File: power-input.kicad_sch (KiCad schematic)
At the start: 23 parts, among them J802 Conn_01x04, U202 XL1509-3.3

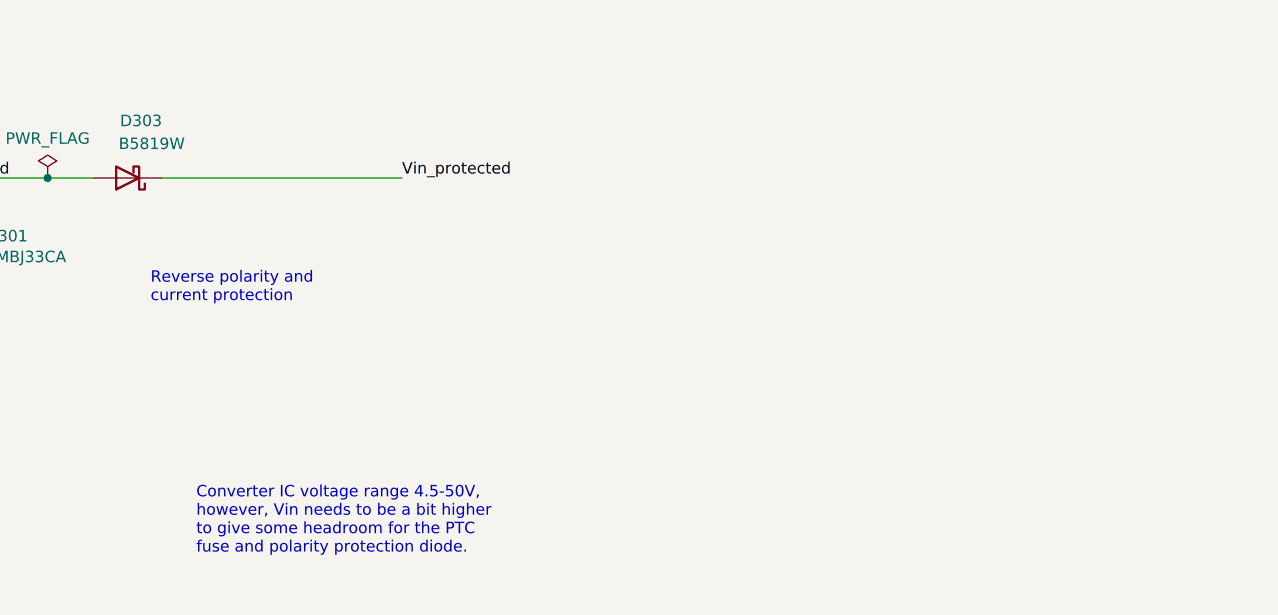
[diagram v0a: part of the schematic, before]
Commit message: Initial V1.0.0 Bluefin forked
Added ICM-42688-P 6-axis IMU
Added LM317 LDO for 6.4v or 5v MHU supply (selectable via jumper)
Added External LED's for IO2 (Pin 24) and 3.3v
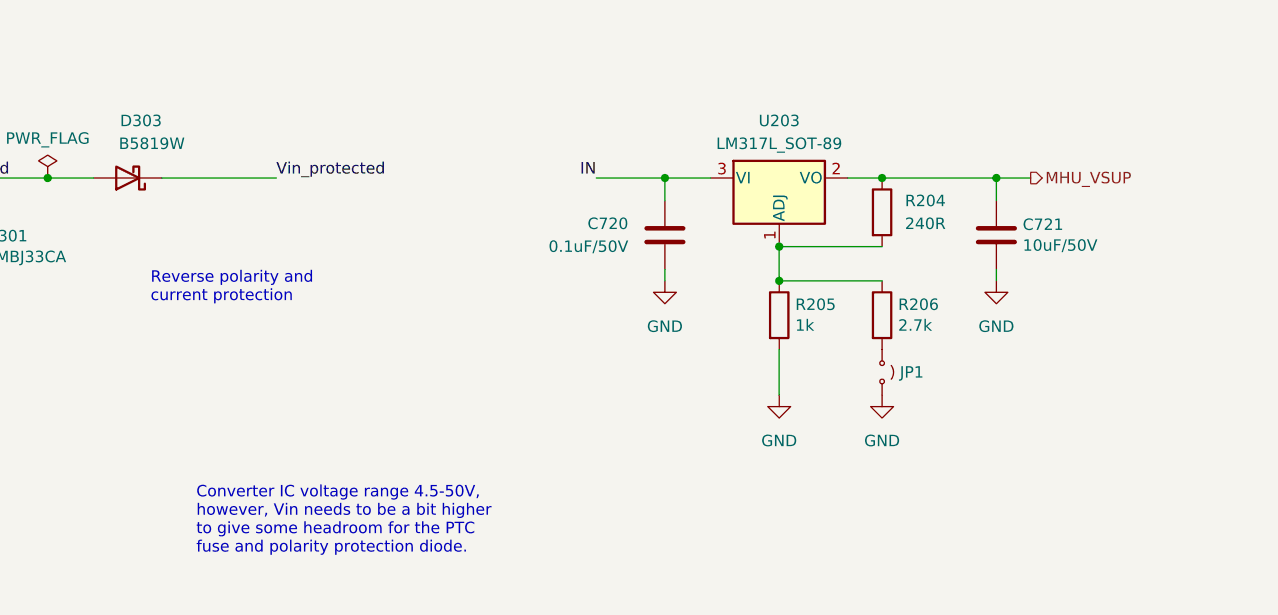
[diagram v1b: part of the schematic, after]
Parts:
- added C720: 0.1uF/50V, Capacitor_SMD:C_1206_3216Metric, symbol Device:C
- added C721: 10uF/50V, Capacitor_SMD:C_1206_3216Metric, symbol Device:C
- added JP1: Jumper_2_Small_Open, Connector_PinHeader_1.00mm:PinHeader_1x02_P1.00mm_Vertical, symbol Jumper:Jumper_2_Small_Open
- added R204: 240R, Resistor_SMD:R_0402_1005Metric, symbol Device:R
- added R205: 1k, Resistor_SMD:R_0402_1005Metric, symbol Device:R
- added R206: 2.7k, Resistor_SMD:R_0402_1005Metric, symbol Device:R
- added U203: LM317L_SOT-89, Package_TO_SOT_SMD:SOT-89-3, symbol Regulator_Linear:LM317L_SOT-89
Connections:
- net GND: now also C720.2, C721.2, JP1.2 (B), R205.2
- net IN: now also C720.1, U203.3 (VI)
- new net: JP1.1 (A), R206.2
- new net: R204.2, R205.1, R206.1, U203.1 (ADJ)
- new net MHU_VSUP: C721.1, R204.1, U203.2 (VO)

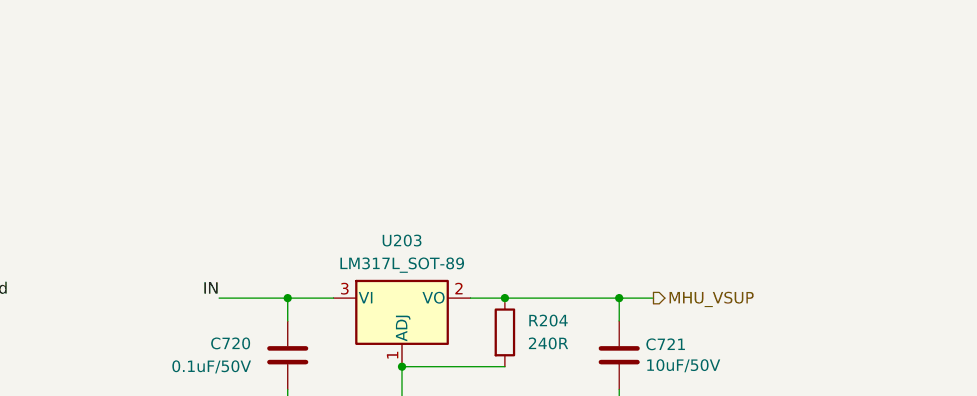
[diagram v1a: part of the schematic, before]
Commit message: Updated LCSC part numbers
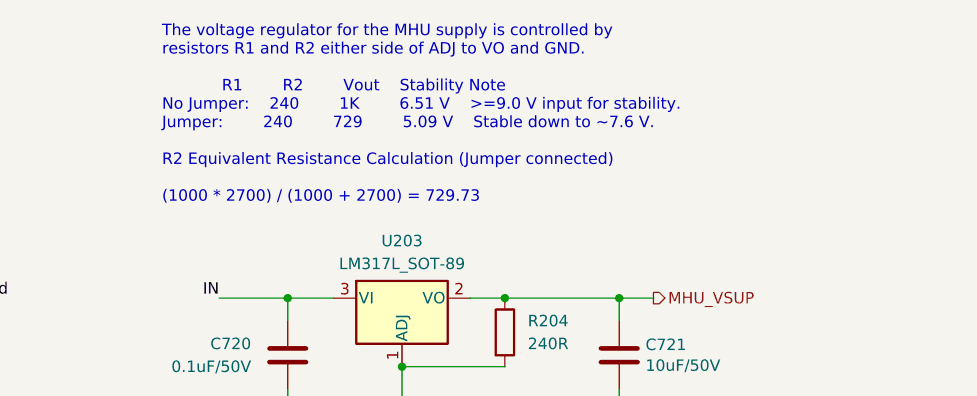
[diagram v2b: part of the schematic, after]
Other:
- note added: "The voltage regulator for the MHU supply is controlled by resistors R1 and R2 either side of ADJ to VO and GND. R1 R2 Vout Stability Note No Jumper: 240 1K 6.51 V >=9.0 V input for stability. Jumper: 240 729 5.09 V Stable down to ~7.6 V. R2 Equivalent Resistance Calculation (Jumper connected) (1000 * 2700) / (1000 + 2700) = 729.73"
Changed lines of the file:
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@@
+		)
+	)
+	(text "The voltage regulator for the MHU supply is controlled by\nresistors R1 and R2 either side of ADJ to VO and GND. \n\n			R1		R2		Vout	Stability Note\nNo Jumper:	240		1K		6.51 V	>=9.0 V input for stability.\nJumper:		240		729		5.09 V	Stable down to ~7.6 V.\n\nR2 Equivalent Resistance Calculation (Jumper connected)\n\n(1000 * 2700) / (1000 + 2700) = 729.73"
+		(exclude_from_sim no)
+		(at 200.66 42.926 0)
+		(effects
+			(font
+				(size 1.27 1.27)
+			)
+			(justify left bottom)
 		)
 	)

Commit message: Moved ESP32-S3 + larger pin headers
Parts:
- JP1: footprint Connector_PinHeader_1.00mm:PinHeader_1x02_P1.00mm_Vertical -> Connector_PinHeader_2.00mm:PinHeader_1x02_P2.00mm_Vertical
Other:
- company: Hat Labs Ltd -> Fifty One North Limited
- title: Hat Labs Marine Engine & Tank interface (HALMET) -> Bluefin Marine Processor
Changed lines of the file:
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@@
 	(paper "A4")
 	(title_block
-		(title "Hat Labs Marine Engine & Tank interface (HALMET)")
-		(date "2024-01-18")
-		(rev "1.0.1")
-		(company "Hat Labs Ltd")
-		(comment 1 "https://creativecommons.org/licenses/by-sa/4.0")
-		(comment 2 "To view a copy of this license, visit ")
-		(comment 3 "HALMET is licensed under CC BY-SA 4.0.")
+		(title "Bluefin Marine Processor")
+		(date "2026-01-08")
+		(rev "1.0.0")
+		(company "Fifty One North Limited")
+		(comment 1 "https://creativecommons.org/licenses/by-sa/4.0/")
+		(comment 2 "Bluefin is licensed under CC BY-SA 4.0")
+		(comment 3 "Modifications © 2026 Fiftyone North Ltd.")
+		(comment 4 "Based on an original design by Hat Labs Ltd.")
 	)
 	(text "Converter IC voltage range 4.5-50V,\nhowever, Vin needs to be a bit higher\nto give some headroom for the PTC\nfuse and polarity protection diode."
@@
 			)
 		)
-		(property "Footprint" "Connector_PinHeader_1.00mm:PinHeader_1x02_P1.00mm_Vertical"
+		(property "Footprint" "Connector_PinHeader_2.00mm:PinHeader_1x02_P2.00mm_Vertical"
 			(at 238.76 74.93 0)
 			(effects

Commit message: Updates LCSC part numbers.
Updates LCSC part numbers in the schematics and PCB to reflect the correct components.

This ensures accurate component sourcing and BOM generation.
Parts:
- JP1: LCSC C36499287 -> C541856
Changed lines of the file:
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@@
 			)
 		)
-		(property "LCSC" "C36499287"
+		(property "LCSC" "C541856"
 			(at 238.76 74.93 90)
 			(effects
